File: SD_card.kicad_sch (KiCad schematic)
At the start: 6 parts, among them J11 TF-15x15

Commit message: I was never here
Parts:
- renumbered R25 to R26, TP18 to TP14, TP19 to TP15, TP20 to TP16, TP21 to TP17
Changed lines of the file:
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@@
   (symbol (lib_id "power:GND") (at 137.16 111.76 0) (unit 1)
     (in_bom yes) (on_board yes)
-    (property "Reference" "#PWR065" (id 0) (at 137.16 118.11 0)
+    (property "Reference" "#PWR068" (id 0) (at 137.16 118.11 0)
       (effects (font (size 1.27 1.27)) hide)
     )
@@
   (symbol (lib_id "power:GND") (at 187.96 111.76 0) (unit 1)
     (in_bom yes) (on_board yes)
-    (property "Reference" "#PWR066" (id 0) (at 187.96 118.11 0)
+    (property "Reference" "#PWR069" (id 0) (at 187.96 118.11 0)
       (effects (font (size 1.27 1.27)) hide)
     )
@@
   (symbol (lib_id "Connector:TestPoint") (at 93.98 91.44 0) (unit 1)
     (in_bom yes) (on_board yes) (fields_autoplaced)
-    (property "Reference" "TP18" (id 0) (at 95.377 87.3033 0)
+    (property "Reference" "TP14" (id 0) (at 95.377 87.3033 0)
       (effects (font (size 1.27 1.27)) (justify left))
     )
@@
   (symbol (lib_id "Device:R") (at 130.81 81.28 90) (unit 1)
     (in_bom yes) (on_board yes)
-    (property "Reference" "R25" (id 0) (at 130.81 76.2 90))
+    (property "Reference" "R26" (id 0) (at 130.81 76.2 90))
     (property "Value" "10k" (id 1) (at 130.81 78.74 90))
     (property "Footprint" "Resistor_SMD:R_0603_1608Metric" (id 2) (at 130.81 83.058 90)
@@
   (symbol (lib_id "Connector:TestPoint") (at 113.03 88.9 0) (unit 1)
     (in_bom yes) (on_board yes) (fields_autoplaced)
-    (property "Reference" "TP20" (id 0) (at 114.427 84.7633 0)
+    (property "Reference" "TP16" (id 0) (at 114.427 84.7633 0)
       (effects (font (size 1.27 1.27)) (justify left))
     )
@@
   (symbol (lib_id "Connector:TestPoint") (at 128.27 101.6 180) (unit 1)
     (in_bom yes) (on_board yes) (fields_autoplaced)
-    (property "Reference" "TP21" (id 0) (at 129.667 104.0673 0)
+    (property "Reference" "TP17" (id 0) (at 129.667 104.0673 0)
       (effects (font (size 1.27 1.27)) (justify right))
     )
@@
   (symbol (lib_id "Connector:TestPoint") (at 110.49 96.52 180) (unit 1)
     (in_bom yes) (on_board yes) (fields_autoplaced)
-    (property "Reference" "TP19" (id 0) (at 111.887 98.9873 0)
+    (property "Reference" "TP15" (id 0) (at 111.887 98.9873 0)
       (effects (font (size 1.27 1.27)) (justify right))
     )

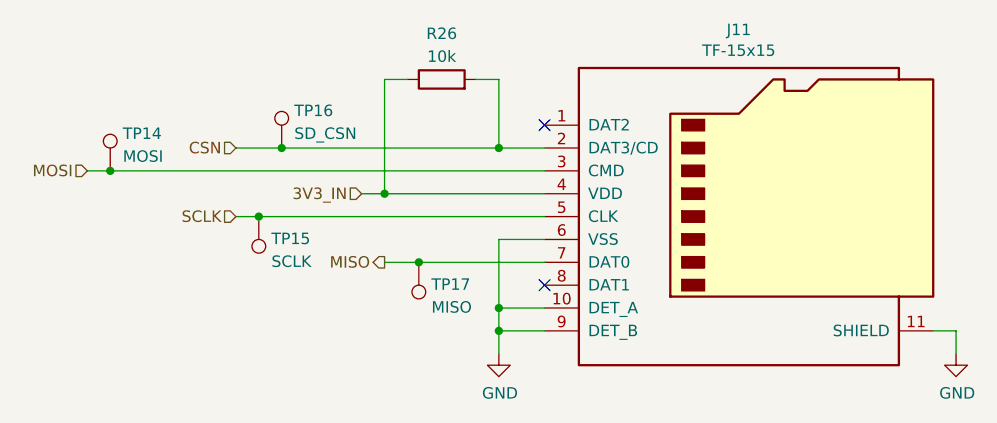
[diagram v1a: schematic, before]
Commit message: Finish routing round 2
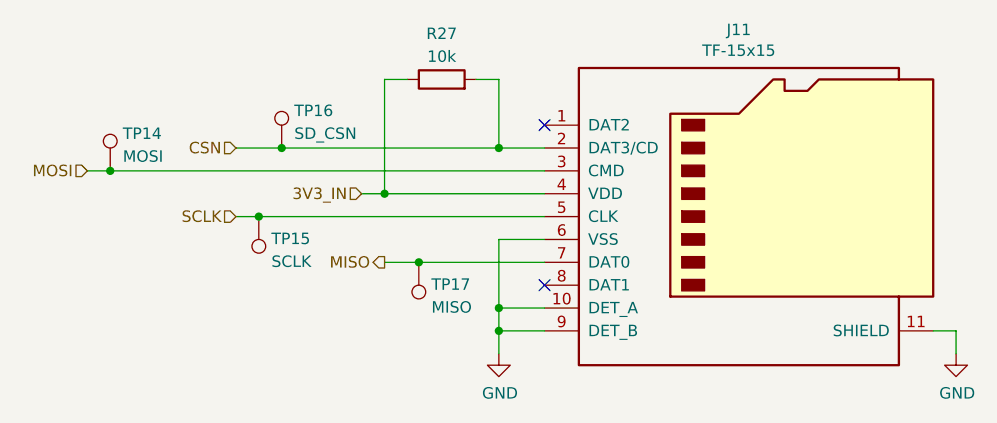
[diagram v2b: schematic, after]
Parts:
- renumbered R26 to R27
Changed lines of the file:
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@@
   (symbol (lib_id "power:GND") (at 137.16 111.76 0) (unit 1)
     (in_bom yes) (on_board yes)
-    (property "Reference" "#PWR068" (id 0) (at 137.16 118.11 0)
+    (property "Reference" "#PWR070" (id 0) (at 137.16 118.11 0)
       (effects (font (size 1.27 1.27)) hide)
     )
@@
   (symbol (lib_id "power:GND") (at 187.96 111.76 0) (unit 1)
     (in_bom yes) (on_board yes)
-    (property "Reference" "#PWR069" (id 0) (at 187.96 118.11 0)
+    (property "Reference" "#PWR071" (id 0) (at 187.96 118.11 0)
       (effects (font (size 1.27 1.27)) hide)
     )
@@
   (symbol (lib_id "Device:R") (at 130.81 81.28 90) (unit 1)
     (in_bom yes) (on_board yes)
-    (property "Reference" "R26" (id 0) (at 130.81 76.2 90))
+    (property "Reference" "R27" (id 0) (at 130.81 76.2 90))
     (property "Value" "10k" (id 1) (at 130.81 78.74 90))
     (property "Footprint" "Resistor_SMD:R_0603_1608Metric" (id 2) (at 130.81 83.058 90)
